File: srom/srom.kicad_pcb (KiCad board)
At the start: 4 copper layers, 100 x 99.8 mm, 32 parts, among them J301 Conn_01x10_Female, J302 Conn_01x06_Female, J304 Conn_01x05_Female, Q1 PMBT2222A, SW101 SW_SPST, SW401 SW_SPST, U1 4075, U101 74LS245, U201 Pico-2 IO, U202 APS6404L-3SQR_PSRAM64Mbit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

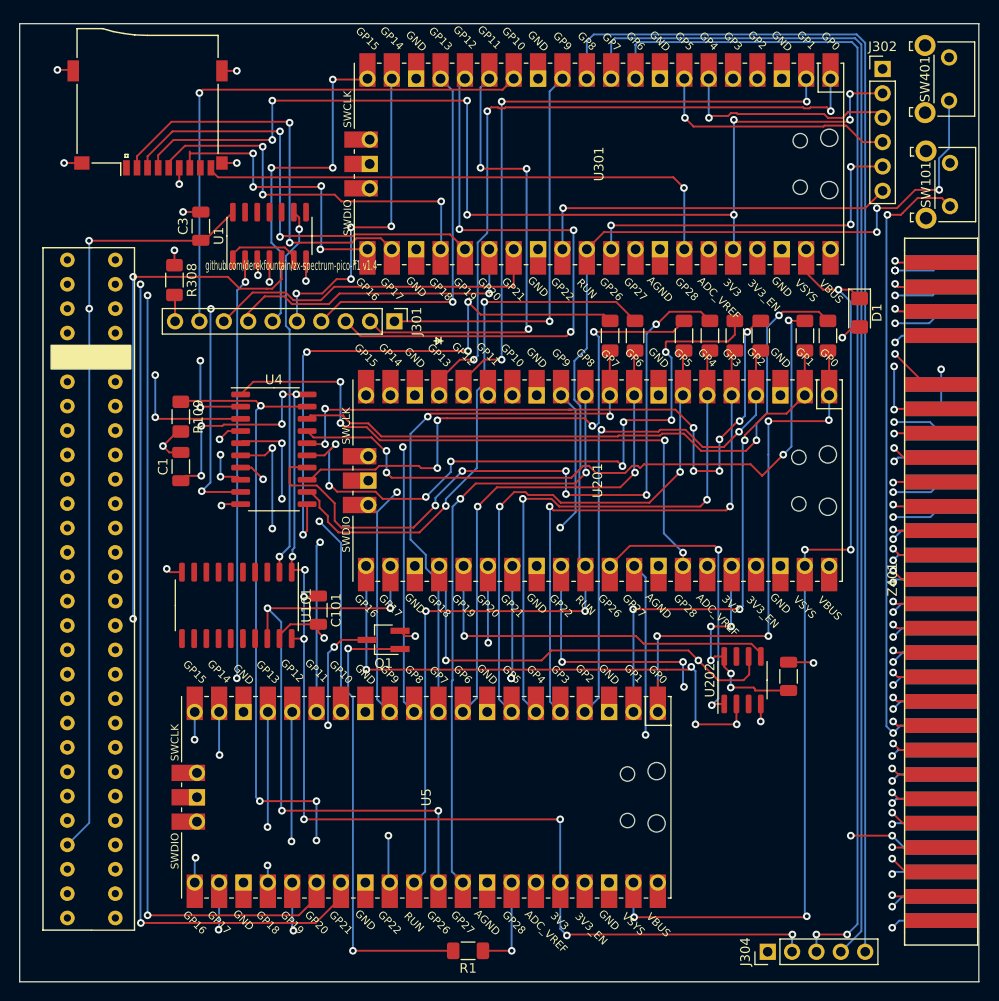
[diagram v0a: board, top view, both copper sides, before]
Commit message: clean ups, test points
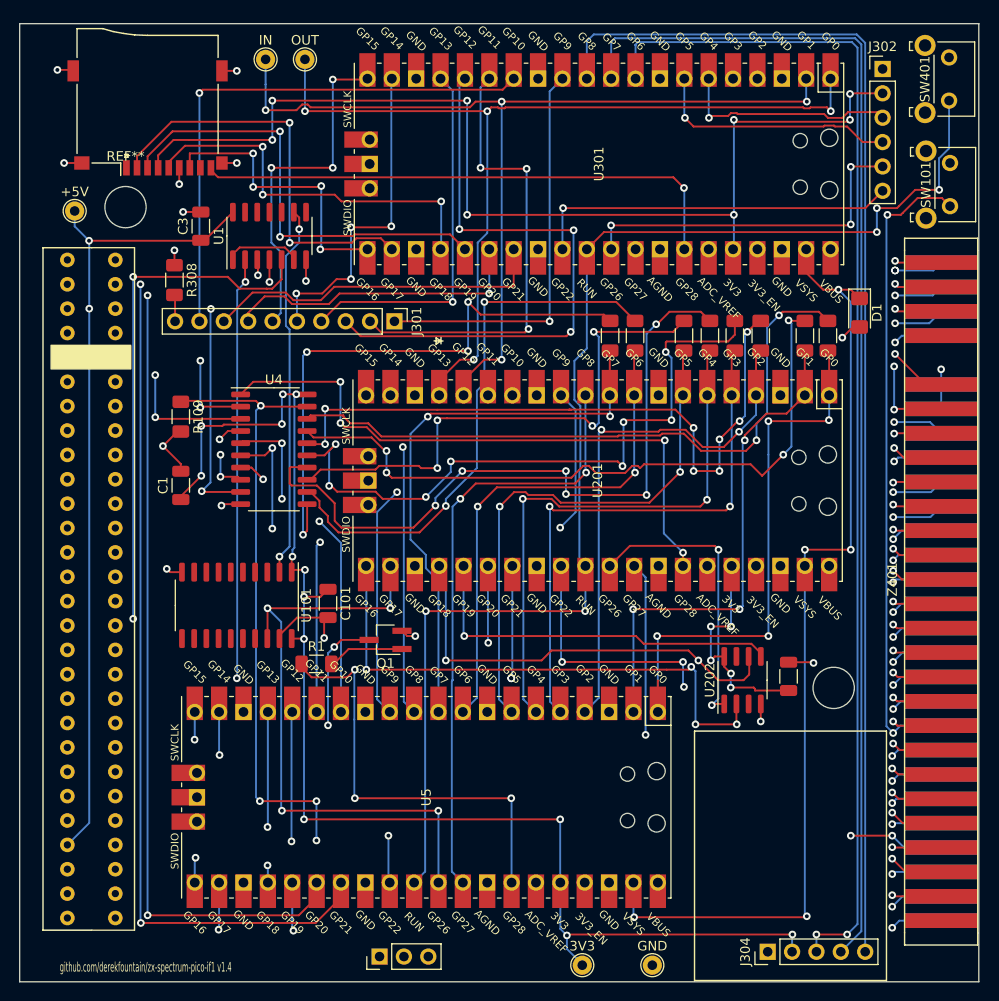
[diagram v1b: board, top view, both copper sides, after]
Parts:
- added +5V: TestPoint_THTPad_D2.0mm_Drill1.0mm, TestPoint:TestPoint_THTPad_D2.0mm_Drill1.0mm, F.Cu at (51.1, 89.7)
- added 3V3: TestPoint_THTPad_D2.0mm_Drill1.0mm, TestPoint:TestPoint_THTPad_D2.0mm_Drill1.0mm, F.Cu at (104.0, 168.3)
- added GND: TestPoint_THTPad_D2.0mm_Drill1.0mm, TestPoint:TestPoint_THTPad_D2.0mm_Drill1.0mm, F.Cu at (111.3, 168.3)
- added IN: TestPoint_THTPad_D2.0mm_Drill1.0mm, TestPoint:TestPoint_THTPad_D2.0mm_Drill1.0mm, F.Cu at (71.0, 73.9)
- added OUT: TestPoint_THTPad_D2.0mm_Drill1.0mm, TestPoint:TestPoint_THTPad_D2.0mm_Drill1.0mm, F.Cu at (75.2, 73.9)
- added REF**: MountingHole_4.3mm_M4, MountingHole:MountingHole_4.3mm_M4, F.Cu at (130.2, 139.4)
- added REF**: MountingHole_4.3mm_M4, MountingHole:MountingHole_4.3mm_M4, F.Cu at (56.5, 89.3)
- added REF**: PinHeader_1x03_P2.54mm_Vertical, Connector_PinHeader_2.54mm:PinHeader_1x03_P2.54mm_Vertical, F.Cu at (82.9, 167.4)
- moved R1 33.8 mm to (76.3, 136.9), turned to 0 degrees
- moved C1 1.97 mm to (62.2, 118.3)
- moved C101 1.22 mm to (77.5, 130.6)
- moved Q1 0.20 mm to (83.5, 134.4)
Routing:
- net Net-(Q1-Pad1): track 47.6 -> 8.00 mm, vias 2 -> 0
- net PICO_RESET_Z80: track 10.1 -> 45.2 mm, vias 1 -> 3
- net UI_LINKIN: track 67.5 -> 98.1 mm, vias 3 -> 4
- net UI_LINKOUT: track 72.2 -> 96.6 mm, vias 3 -> 4
- net 3V3_PICO1: track 135.2 -> 141.2 mm
- net +5V: track 175.9 -> 179.6 mm
- net GND: track 44.5 -> 47.4 mm
- net ZXU: track 94.3 -> 96.4 mm
- net ZXWR: track 113.6 -> 115.7 mm
- net ZXRD: track 144.1 -> 146.2 mm
- net ZXBUSRQ: track 93.1 -> 94.9 mm

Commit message: increase power track widths, more test points, silkscreen tweaks
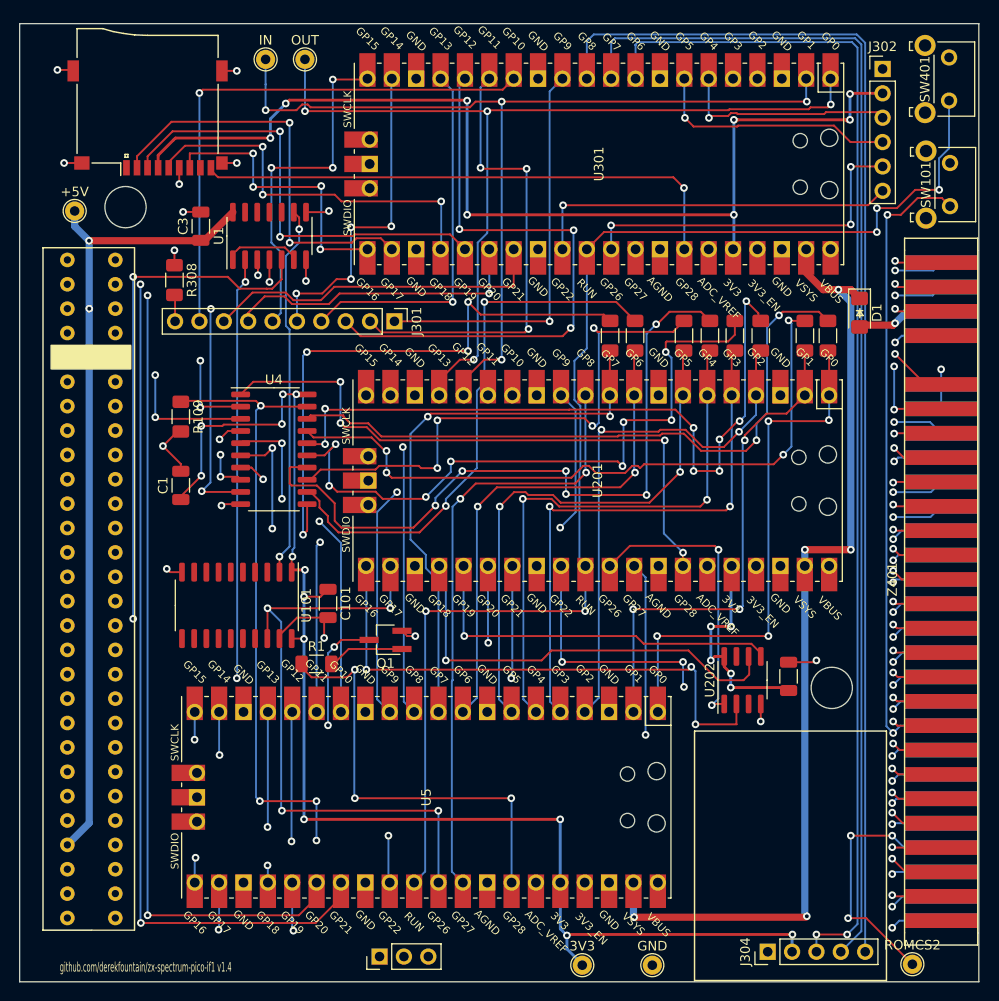
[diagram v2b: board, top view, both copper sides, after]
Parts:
- added ROMCS2: TestPoint_THTPad_D2.0mm_Drill1.0mm, TestPoint:TestPoint_THTPad_D2.0mm_Drill1.0mm, F.Cu at (138.4, 168.2)
- moved REF** 0.20 mm to (130.1, 139.4)
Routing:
- net ROMCS2: track 131.1 -> 148.4 mm, vias 6 -> 7
- net Net-(R103-Pad1): track 70.0 -> 73.5 mm
- net D0: track 58.9 -> 55.4 mm
- net UI_LINKOUT: track 96.6 -> 94.2 mm
- net PICO_PWR: track 101.5 -> 99.1 mm
- net ZXD0: track 98.2 -> 96.6 mm
- net +5V: track 179.6 -> 181.2 mm, vias 4 -> 3
- net ZXA13: track 179.3 -> 177.7 mm
- net ZXA12: track 178.5 -> 177.0 mm
- net UI_LINKIN: track 98.1 -> 96.5 mm
- net GND: track 47.4 -> 48.6 mm, vias 17 -> 18
- net 3V3_PICO3: track 109.9 -> 108.7 mm
- net Net-(R102-Pad1): track 72.0 -> 71.0 mm
- net ZXA14: track 96.5 -> 95.7 mm, vias 3 -> 2
- net ZXVIDEO: track 94.4 -> 93.7 mm
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
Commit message: final pcb? about to copy layout for daughterboard
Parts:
- added BL2: TestPoint_THTPad_D2.0mm_Drill1.0mm, TestPoint:TestPoint_THTPad_D2.0mm_Drill1.0mm, F.Cu at (71.0, 105.7)
- added BL3: TestPoint_THTPad_D2.0mm_Drill1.0mm, TestPoint:TestPoint_THTPad_D2.0mm_Drill1.0mm, F.Cu at (70.8, 73.8)
- moved REF** 23.9 mm to (106.8, 168.0)
- moved GND 14.9 mm to (96.5, 168.2)
- moved 3V3 12.4 mm to (91.7, 168.2)
- moved IN 2.70 mm to (73.8, 73.8)
- moved OUT 1.80 mm to (77.0, 73.9)
- moved +5V 0.90 mm to (50.2, 89.7)
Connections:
- U301 pad 6: OLED_SCK -> OLED_SDA
- U301 pad 7: OLED_SDA -> OLED_SCK
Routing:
- net TEST_BLIPPER_P2: track 0.00 -> 31.1 mm
- net 3V3_PICO1: track 140.8 -> 149.3 mm
- net TEST_BLIPPER_P3: track 57.2 -> 61.0 mm, vias 1 -> 2
- net OLED_SCK: track 22.8 -> 26.3 mm
- net UI_LINKIN: track 96.5 -> 99.1 mm
- net ZXD0: track 96.6 -> 98.2 mm
- net UI_LINKOUT: track 94.2 -> 95.8 mm
- net ZXD1: track 105.7 -> 104.8 mm
- net OLED_SDA: track 25.8 -> 26.5 mm

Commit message: lots more work to finalise the board pre-fab
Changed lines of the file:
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@@
     )
     (pad_to_mask_clearance 0)
-    (grid_origin 47.85 91.94)
+    (grid_origin 45.45 70.24)
     (pcbplotparams
       (layerselection 0x00010fc_ffffffff)
@@
   (gr_circle (center 131.25 105.54) (end 131.391421 105.54) (layer "F.SilkS") (width 0.15) (fill solid))
   (gr_line (start 132.975 100.14) (end 132.675 100.63) (layer "F.SilkS") (width 0.15))
+  (gr_circle (center 66.95 107.54) (end 67.091421 107.54) (layer "F.SilkS") (width 0.15) (fill solid))
   (gr_circle (center 142.35 82.64) (end 142.491421 82.64) (layer "F.SilkS") (width 0.15) (fill solid))
   (gr_line (start 132.615 100.13) (end 133.285 100.13) (layer "F.SilkS") (width 0.15))
@@
   (gr_circle (center 131.75 73.64) (end 131.891421 73.64) (layer "F.SilkS") (width 0.15) (fill solid))
   (gr_line (start 132.635 100.64) (end 133.315 100.64) (layer "F.SilkS") (width 0.15))
+  (gr_rect (start 77.95 112.74) (end 85.45 122.74) (layer "Dwgs.User") (width 0.15) (fill none))
+  (gr_rect (start 77.95 80.24) (end 85.45 90.24) (layer "Dwgs.User") (width 0.15) (fill none))
   (gr_rect (start 45.42 70.22) (end 145.38 170.07) (layer "Edge.Cuts") (width 0.1) (fill none))
   (gr_line (start 82.52 88.92) (end 82.61 88.87) (layer "User.1") (width 0.15))
